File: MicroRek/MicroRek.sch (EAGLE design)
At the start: 18 parts, among them IC3 LSM9DS1TR

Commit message: LOTS of work on board layout
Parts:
- added LED1, LED2, LED3: (no value), led:LEDCHIPLED_0805
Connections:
- removed net D2_5: U$1.PD2[D2]
- removed net N$7: C7.1, IC3.VDDIO1, IC3.VDDIO2
- new net N$6: IC3.VDD1, IC3.VDD2
- net 3.3V: now also C7.1, IC3.VDDIO1, IC3.VDDIO2
- net D25: now also U$1.PD2[D2]
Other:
- note added: "0805 LED"
- note added: "100ohm for R3 100kohm for R2 4.7kohm R1 For LEDS"
- note added: "4.7k Pull up on both sides"
- note added: "Change inductor package"
- note added: "Check if capacitors are needed"
- note added: "Make lines equal length and straight"
- note added: "Pull up resistors needed"
- note added: "Reset needs to go to programming port"
- note added: "Run to 3.3"
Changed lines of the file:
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@@
 <part name="U$1" library="CPSS_CPU" deviceset="ATMEGA328P" device=""/>
 <part name="GND20" library="supply1" library_urn="urn:adsk.eagle:library:371" deviceset="GND" device=""/>
+<part name="LED1" library="led" library_urn="urn:adsk.eagle:library:259" deviceset="LED" device="CHIPLED_0805" package3d_urn="urn:adsk.eagle:package:15821/2"/>
+<part name="LED2" library="led" library_urn="urn:adsk.eagle:library:259" deviceset="LED" device="CHIPLED_0805" package3d_urn="urn:adsk.eagle:package:15821/2"/>
+<part name="LED3" library="led" library_urn="urn:adsk.eagle:library:259" deviceset="LED" device="CHIPLED_0805" package3d_urn="urn:adsk.eagle:package:15821/2"/>
 </parts>
 <sheets>
@@
 <plain>
 <frame x1="0" y1="0" x2="279.4" y2="215.9" columns="8" rows="5" layer="97"/>
+<circle x="246.38" y="149.86" radius="7.184203125" width="0.1524" layer="101"/>
+<circle x="81.28" y="144.78" radius="10.4726875" width="0.1524" layer="101"/>
+<text x="33.02" y="78.74" size="1.778" layer="101">4.7k Pull up on both sides</text>
+<circle x="165.1" y="177.8" radius="8.032184375" width="0.1524" layer="101"/>
+<text x="259.08" y="149.86" size="1.778" layer="101">Run to 3.3</text>
+<text x="96.52" y="142.24" size="1.778" layer="101">Make lines equal length and straight</text>
+<text x="162.56" y="175.26" size="1.778" layer="101">Pull up resistors needed</text>
+<text x="226.06" y="124.46" size="1.778" layer="101">Pull up resistors needed</text>
+<circle x="231.14" y="119.38" radius="9.1581" width="0.1524" layer="101"/>
+<text x="96.52" y="137.16" size="1.778" layer="101">Check if capacitors are needed</text>
+<circle x="96.52" y="109.22" radius="9.1581" width="0.1524" layer="101"/>
+<text x="99.06" y="114.3" size="1.778" layer="101">Change inductor package</text>
+<text x="144.78" y="55.88" size="1.778" layer="101">100ohm for R3
+100kohm for R2
+4.7kohm R1
+For LEDS</text>
+<text x="147.32" y="33.02" size="1.778" layer="101">0805 LED</text>
+<text x="160.02" y="172.72" size="1.778" layer="101">Reset needs to go to programming port</text>
 </plain>
 <instances>
@@
 <instance part="U$1" gate="G$1" x="127" y="172.72"/>
 <instance part="GND20" gate="1" x="88.9" y="175.26"/>
+<instance part="LED1" gate="G$1" x="203.2" y="50.8"/>
+<instance part="LED2" gate="G$1" x="210.82" y="40.64"/>
+<instance part="LED3" gate="G$1" x="220.98" y="53.34"/>
 </instances>
 <busses>
@@
 <label x="10.16" y="187.96" size="1.778" layer="95"/>
 </segment>
-</net>
-<net name="N$7" class="0">
 <segment>
 <pinref part="IC3" gate="G$1" pin="VDDIO1"/>
@@
 <junction x="190.5" y="187.96"/>
 <pinref part="C7" gate="G$1" pin="1"/>
+<label x="180.34" y="198.12" size="1.778" layer="95"/>
+<wire x1="190.5" y1="198.12" x2="180.34" y2="198.12" width="0.1524" layer="91"/>
+<junction x="190.5" y="198.12"/>
 </segment>
 </net>
@@
 <label x="68.58" y="43.18" size="1.778" layer="95"/>
 </segment>
-</net>
-<net name="D2_5" class="0">
 <segment>
 <pinref part="U$1" gate="G$1" pin="PD2[D2]"/>
@@
 <wire x1="154.94" y1="177.8" x2="167.64" y2="177.8" width="0.1524" layer="91"/>
 <label x="162.56" y="177.8" size="1.778" layer="95"/>
+</segment>
+</net>
+<net name="N$6" class="0">
+<segment>
+<pinref part="IC3" gate="G$1" pin="VDD1"/>
+<wire x1="243.84" y1="152.4" x2="248.92" y2="152.4" width="0.1524" layer="91"/>
+<wire x1="248.92" y1="152.4" x2="248.92" y2="147.32" width="0.1524" layer="91"/>
+<pinref part="IC3" gate="G$1" pin="VDD2"/>
+<wire x1="248.92" y1="147.32" x2="243.84" y2="147.32" width="0.1524" layer="91"/>
 </segment>
 </net>
@@
 </drawing>
 <compatibility>
+<note version="6.3" minversion="6.2.2" severity="warning">
+Since Version 6.2.2 text objects can contain more than one line,
+which will not be processed correctly with this version.
+</note>
 <note version="8.2" severity="warning">
 Since Version 8.2, EAGLE supports online libraries. The ids

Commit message: MicroRek Updates
Changed inductor package
Fixed some wiring
Fixed Crystal wiring (MAYBE)
Will work more in the morning
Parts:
- L1: device resistor:L-US0204/5 -> CPSS:L-US
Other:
- note added: "Make lines equal length and straight I tried to make them equal but I'm not sure how I can get them straight. They don't line up if they are on the same layer so I need to use a via and that means they can't be perectly straight I looked at dathseet don't see anything about capacitors"
- note removed: "Change inductor package"
- note removed: "Check if capacitors are needed"
- note removed: "Make lines equal length and straight"

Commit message: Board Updates
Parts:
- added R2: 100Ω, resistor:R-US_R0603
- added R3: 100kΩ, resistor:R-US_R0603
- added R4: 4.7kΩ, resistor:R-US_R0603
- added R5, R6, R7, R8: 10kΩ, resistor:R-US_R0603
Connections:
- net 3.3V: now also IC3.VDD1, IC3.VDD2, R4.1
- net 5V: now also R5.2, R6.2, R7.1, R8.1
- net GND: now also R2.1, R2.2, R3.1, R4.2
- net N$6: now also LED1.C, R3.2; no longer IC3.VDD1, IC3.VDD2
- net SCL3: now also R8.2
- net SCL5: now also R6.1
- net SDA3: now also R7.2
- net SDA5: now also R5.1
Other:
- note removed: "Make lines equal length and straight I tried to make them equal but I'm not sure how I can get them straight. They don't line up if they are on the same layer so I need to use a via and that means they can't be perectly straight I looked at dathseet don't see anything about capacitors"
- note removed: "Pull up resistors needed"
- note removed: "Run to 3.3"
- moved on the sheet: LED1

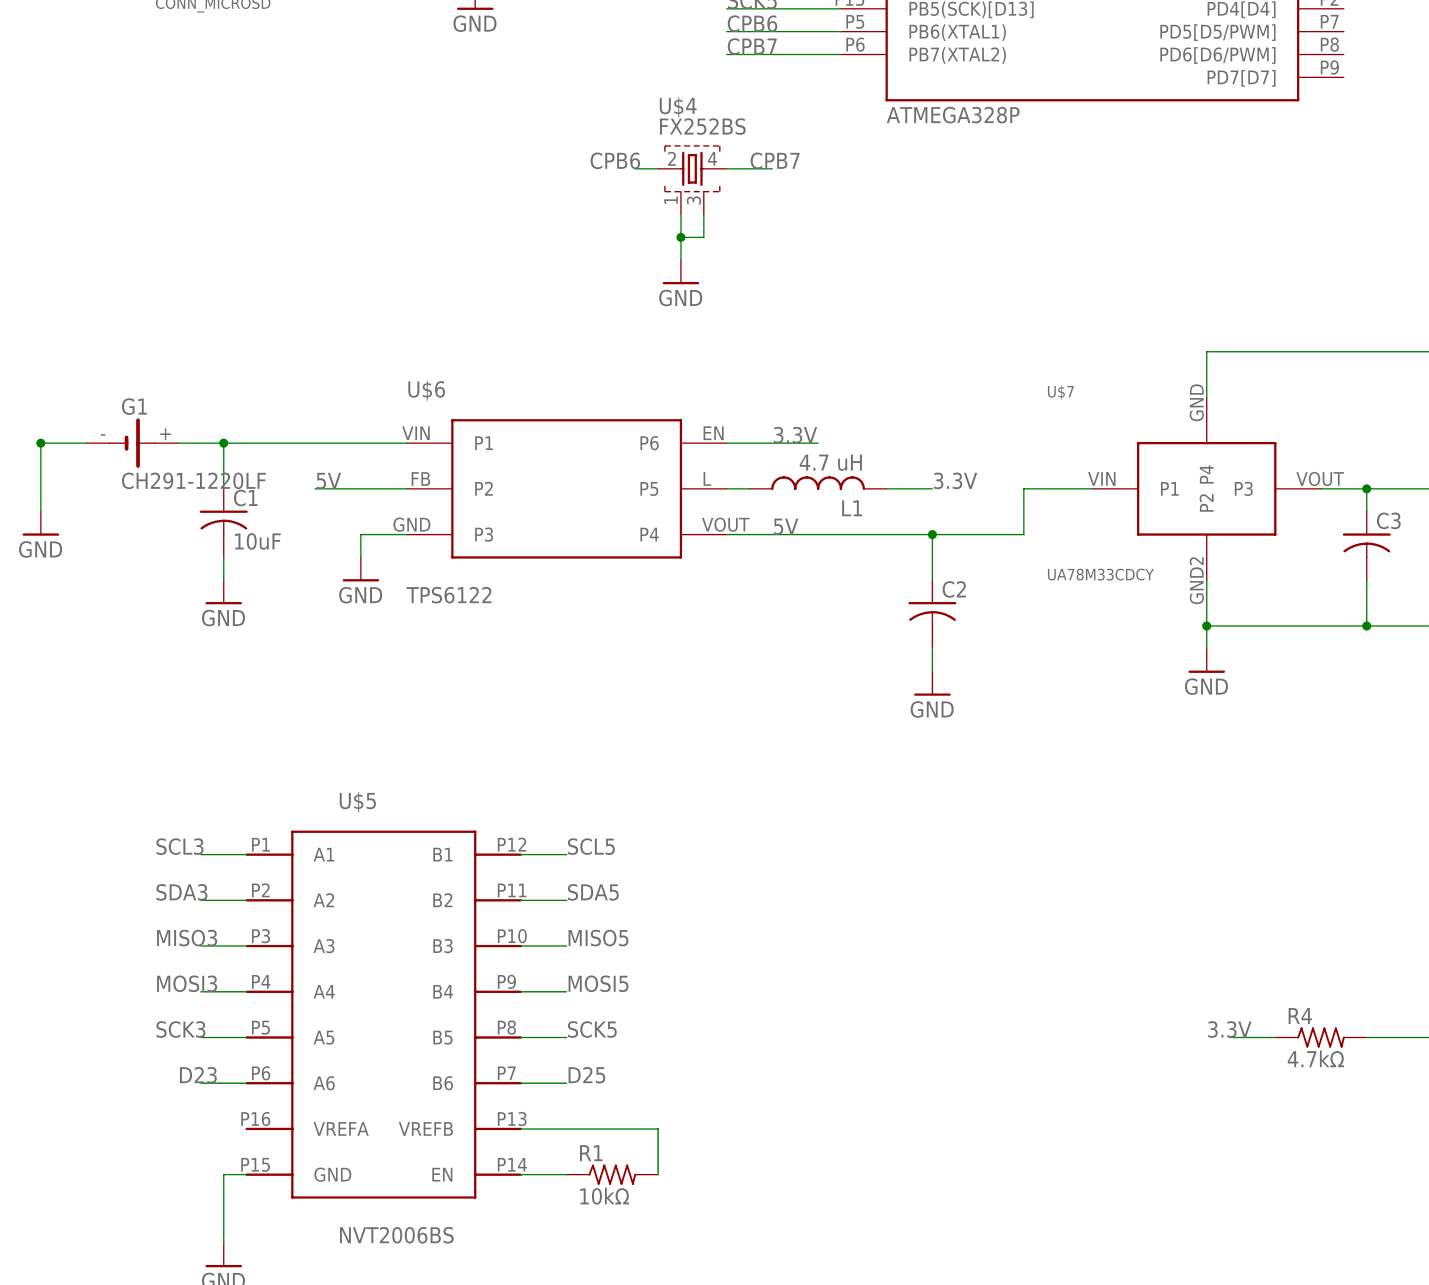
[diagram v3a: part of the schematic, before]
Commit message: MicroRek Update
Added pullup resistors and the mini icsp port
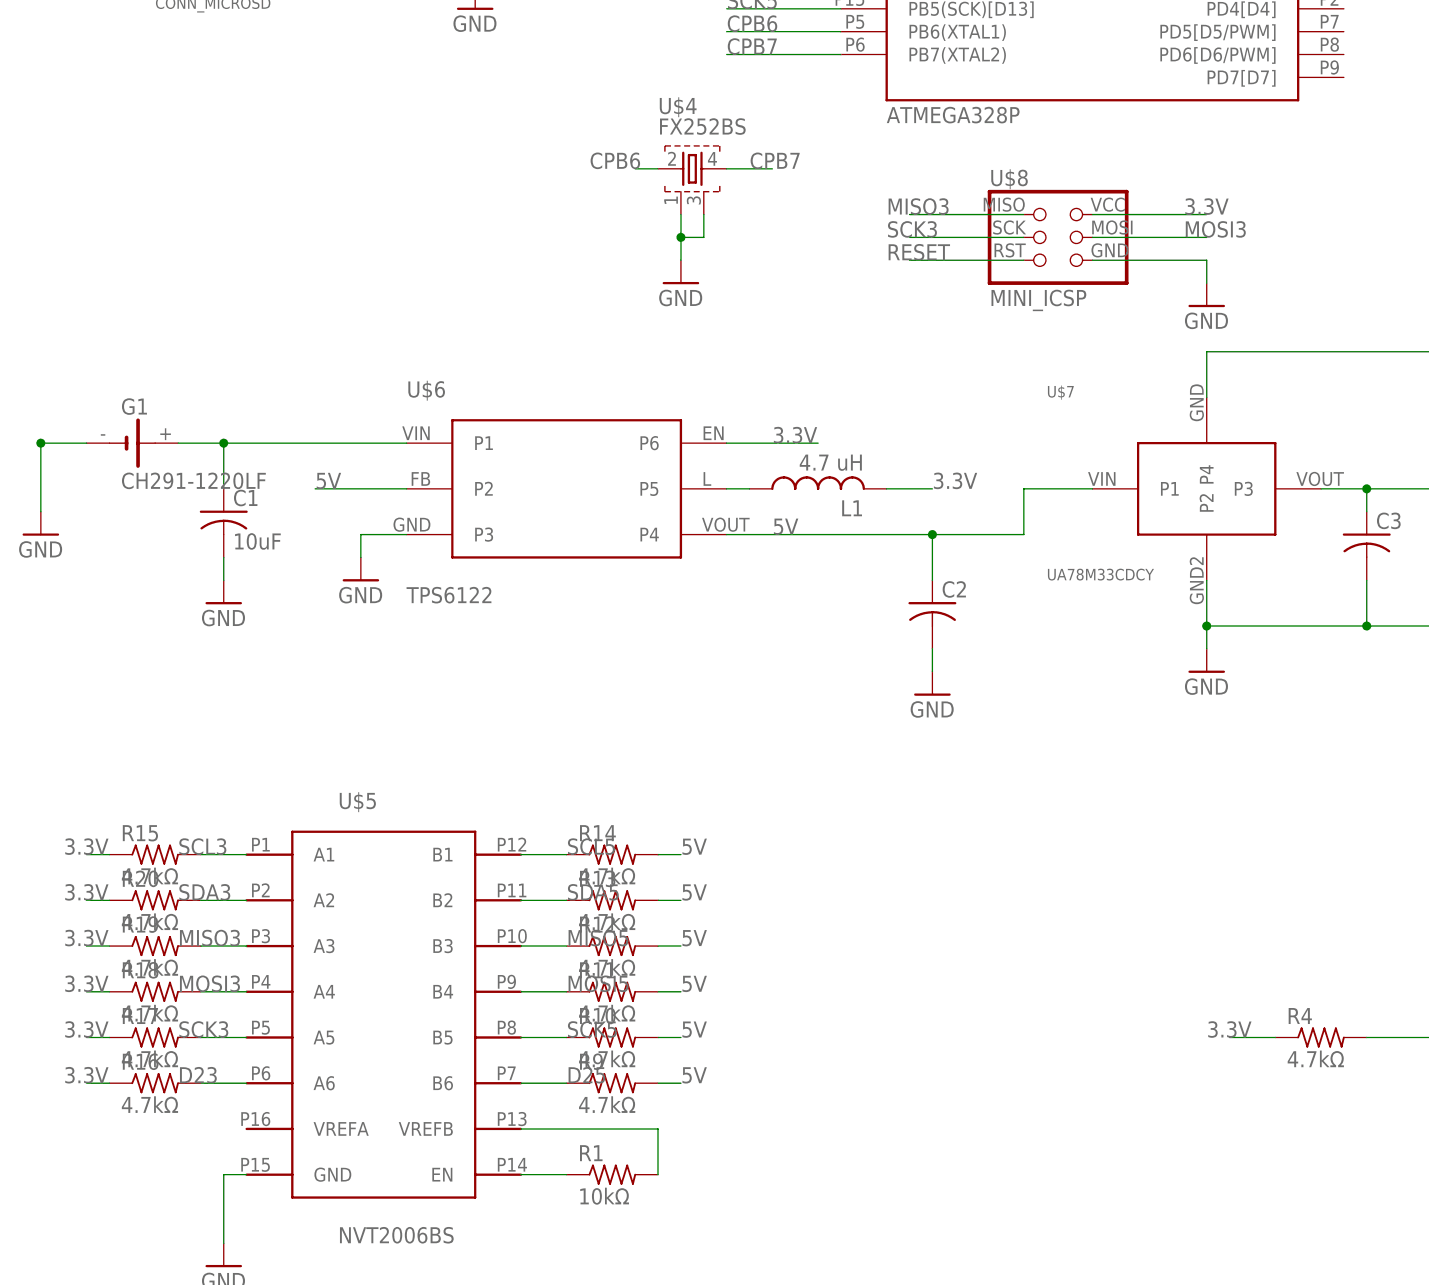
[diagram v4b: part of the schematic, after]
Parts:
- added R10, R11, R12, R13, R14, R15, R16, R17, R18, R19, R20, R9: 4.7kΩ, resistor:R-US_R0603
- added U$8: MINI_ICSP, CPSS_CONNECTOR:MINI_ICSP
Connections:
- net 3.3V: now also R15.1, R16.1, R17.1, R18.1, R19.1, R20.1, U$8.2
- net 5V: now also R10.2, R11.2, R12.2, R13.2, R14.2, R9.2
- net D23: now also R16.2
- net D25: now also R9.1
- net GND: now also U$8.6
- net MISO3: now also R19.2, U$8.1
- net MISO5: now also R12.1
- net MOSI3: now also R18.2, U$8.4
- net MOSI5: now also R11.1
- net RESET: now also U$8.5
- net SCK3: now also R17.2, U$8.3
- net SCK5: now also R10.1
- net SCL3: now also R15.2
- net SCL5: now also R14.1
- net SDA3: now also R20.2
- net SDA5: now also R13.1
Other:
- note removed: "Reset needs to go to programming port"
